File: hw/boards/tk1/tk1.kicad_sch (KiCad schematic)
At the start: 0 parts

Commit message: TK-1 release
* Add dimensions for PCB
* Add layer stackup for PCB
* Change PCB component origin to match expanded board
* Change schematic title to 'TK-1', update release date
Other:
- note added: "Tillitis TK-1"
- note removed: "Tillitis TK1"
- title: TK1 -> TK-1
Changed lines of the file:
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@@
   (paper "A4")
   (title_block
-    (title "TK1")
-    (date "2021-09-29")
+    (title "TK-1")
+    (date "2021-11-14")
     (rev "V1")
     (company "Tillitis AB")
@@
     (effects (font (size 1.27 1.27)) (justify left bottom))
   )
-  (text "Tillitis TK1" (at 106.68 24.13 0)
+  (text "Tillitis TK-1" (at 106.68 24.13 0)
     (effects (font (size 6 6) (thickness 0.254) bold) (justify left bottom))
   )
@@
     )
     (path "/00000000-0000-0000-0000-0000611a4eb9/00000000-0000-0000-0000-000061804e06"
-      (reference "TP1") (unit 1) (value "5V") (footprint "TestPoint:TestPoint_Pad_D1.0mm")
+      (reference "TP1") (unit 1) (value "5V") (footprint "mta1:TestPoint_Pad_D1.0mm")
     )
     (path "/00000000-0000-0000-0000-0000611a4eb9/00000000-0000-0000-0000-000061290a70"
-      (reference "TP2") (unit 1) (value "3V3") (footprint "TestPoint:TestPoint_Pad_D1.0mm")
+      (reference "TP2") (unit 1) (value "3V3") (footprint "mta1:TestPoint_Pad_D1.0mm")
     )
     (path "/00000000-0000-0000-0000-0000611a4eb9/00000000-0000-0000-0000-000061293ed2"
-      (reference "TP3") (unit 1) (value "2V5") (footprint "TestPoint:TestPoint_Pad_D1.0mm")
+      (reference "TP3") (unit 1) (value "2V5") (footprint "mta1:TestPoint_Pad_D1.0mm")
     )
     (path "/00000000-0000-0000-0000-0000611a4eb9/00000000-0000-0000-0000-0000612c6885"
-      (reference "TP4") (unit 1) (value "1V2") (footprint "TestPoint:TestPoint_Pad_D1.0mm")
+      (reference "TP4") (unit 1) (value "1V2") (footprint "mta1:TestPoint_Pad_D1.0mm")
     )
     (path "/00000000-0000-0000-0000-0000611cc101/ab35f289-cbe7-449b-a15d-459a3b4e9240"
-      (reference "TP5") (unit 1) (value "APP_GND") (footprint "TestPoint:TestPoint_Pad_D1.0mm")
+      (reference "TP5") (unit 1) (value "APP_GND") (footprint "mta1:TestPoint_Pad_D1.0mm")
     )
     (path "/00000000-0000-0000-0000-00006161400b/fb64afad-a905-4f4b-98a2-d21a64bd12f3"
-      (reference "TP6") (unit 1) (value "INT_TX") (footprint "TestPoint:TestPoint_Pad_D1.0mm")
+      (reference "TP6") (unit 1) (value "INT_TX") (footprint "mta1:TestPoint_Pad_D1.0mm")
     )
     (path "/00000000-0000-0000-0000-00006161400b/1f54ffea-0a26-464d-98d4-30979db7344f"
-      (reference "TP7") (unit 1) (value "INT_RX") (footprint "TestPoint:TestPoint_Pad_D1.0mm")
+      (reference "TP7") (unit 1) (value "INT_RX") (footprint "mta1:TestPoint_Pad_D1.0mm")
     )
     (path "/00000000-0000-0000-0000-00006161400b/74f30866-0d52-4558-88d9-da85c982a4ac"
-      (reference "TP8") (unit 1) (value "INT_RTS") (footprint "TestPoint:TestPoint_Pad_D1.0mm")
+      (reference "TP8") (unit 1) (value "INT_RTS") (footprint "mta1:TestPoint_Pad_D1.0mm")
     )
     (path "/00000000-0000-0000-0000-00006161400b/d9fa1bba-ba87-4376-952a-41bb8392f957"
-      (reference "TP9") (unit 1) (value "INT_CTS") (footprint "TestPoint:TestPoint_Pad_D1.0mm")
+      (reference "TP9") (unit 1) (value "INT_CTS") (footprint "mta1:TestPoint_Pad_D1.0mm")
     )
     (path "/00000000-0000-0000-0000-0000611cc101/b84f4f68-cc10-43a0-962e-10a1890e7eaf"
-      (reference "TP12") (unit 1) (value "APP_ICE_SCK") (footprint "TestPoint:TestPoint_Pad_D1.0mm")
+      (reference "TP12") (unit 1) (value "APP_ICE_SCK") (footprint "mta1:TestPoint_Pad_D1.0mm")
     )
     (path "/00000000-0000-0000-0000-0000611cc101/f77c0061-34af-41f5-8a00-bb8ae07fe922"
-      (reference "TP13") (unit 1) (value "APP_ICE_SS") (footprint "TestPoint:TestPoint_Pad_D1.0mm")
+      (reference "TP13") (unit 1) (value "APP_ICE_SS") (footprint "mta1:TestPoint_Pad_D1.0mm")
     )
     (path "/00000000-0000-0000-0000-0000611cc101/3c9864fc-0a77-4fe0-8c96-c0260a516ba1"
-      (reference "TP14") (unit 1) (value "APP_ICE_MOSI") (footprint "TestPoint:TestPoint_Pad_D1.0mm")
+      (reference "TP14") (unit 1) (value "APP_ICE_MOSI") (footprint "mta1:TestPoint_Pad_D1.0mm")
     )
     (path "/00000000-0000-0000-0000-0000611cc101/0f9d611d-221f-42fe-a161-07c0ff52c542"
-      (reference "TP15") (unit 1) (value "APP_ICE_MISO") (footprint "TestPoint:TestPoint_Pad_D1.0mm")
+      (reference "TP15") (unit 1) (value "APP_ICE_MISO") (footprint "mta1:TestPoint_Pad_D1.0mm")
     )
     (path "/00000000-0000-0000-0000-0000611cc101/d7bf813c-bb4e-4ed8-b86f-d9ec1d86656d"
-      (reference "TP16") (unit 1) (value "APP_CRESET") (footprint "TestPoint:TestPoint_Pad_D1.0mm")
+      (reference "TP16") (unit 1) (value "APP_CRESET") (footprint "mta1:TestPoint_Pad_D1.0mm")
     )
     (path "/00000000-0000-0000-0000-0000611cc101/32f54cf3-1e0f-4aaa-b508-267b9568217c"
-      (reference "TP17") (unit 1) (value "APP_CDONE") (footprint "TestPoint:TestPoint_Pad_D1.0mm")
+      (reference "TP17") (unit 1) (value "APP_CDONE") (footprint "mta1:TestPoint_Pad_D1.0mm")
     )
     (path "/00000000-0000-0000-0000-0000611cc101/e7d44998-7d27-4371-9f3d-0a968eddee9d"
-      (reference "TP18") (unit 1) (value "APP_GPIO1") (footprint "TestPoint:TestPoint_Pad_D1.0mm")
+      (reference "TP18") (unit 1) (value "APP_GPIO1") (footprint "mta1:TestPoint_Pad_D1.0mm")
     )
     (path "/00000000-0000-0000-0000-0000611cc101/855a271d-d14e-4340-88ef-5eb1d2805d77"
-      (reference "TP19") (unit 1) (value "APP_GPIO2") (footprint "TestPoint:TestPoint_Pad_D1.0mm")
+      (reference "TP19") (unit 1) (value "APP_GPIO2") (footprint "mta1:TestPoint_Pad_D1.0mm")
     )
     (path "/00000000-0000-0000-0000-0000611cc101/8aa5c85f-46b3-4ac4-bd48-3e3352ebb3f6"
-      (reference "TP20") (unit 1) (value "APP_GPIO3") (footprint "TestPoint:TestPoint_Pad_D1.0mm")
+      (reference "TP20") (unit 1) (value "APP_GPIO3") (footprint "mta1:TestPoint_Pad_D1.0mm")
     )
     (path "/00000000-0000-0000-0000-0000611cc101/a6d52094-2dbe-49fa-99c1-8b125d3ae4c6"
-      (reference "TP21") (unit 1) (value "APP_GPIO4") (footprint "TestPoint:TestPoint_Pad_D1.0mm")
+      (reference "TP21") (unit 1) (value "APP_GPIO4") (footprint "mta1:TestPoint_Pad_D1.0mm")
     )
     (path "/00000000-0000-0000-0000-0000611a4eb9/f74c1147-0f6c-4852-95d4-43a254720c79"
-      (reference "TP28") (unit 1) (value "GND") (footprint "TestPoint:TestPoint_Pad_D1.0mm")
+      (reference "TP28") (unit 1) (value "GND") (footprint "mta1:TestPoint_Pad_D1.0mm")
     )
     (path "/00000000-0000-0000-0000-0000611a4eb9/00000000-0000-0000-0000-00006126a5e3"

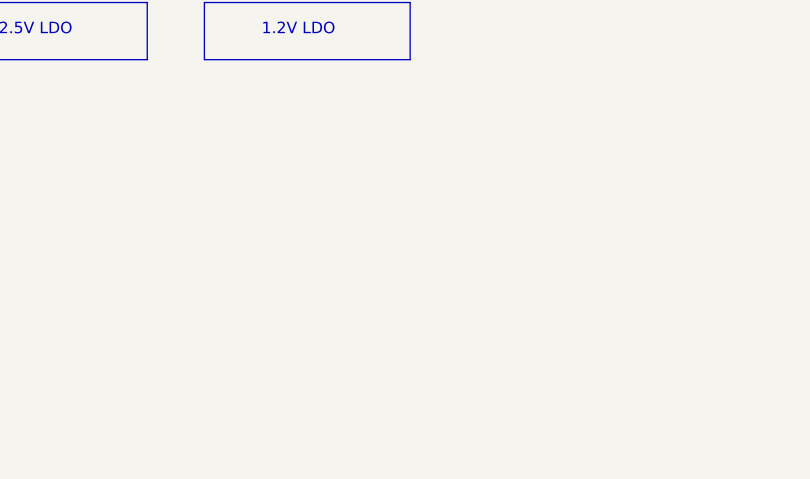
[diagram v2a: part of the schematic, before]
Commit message: TK-1: RevA.1 release
* Add two fiducials to TK-1 board
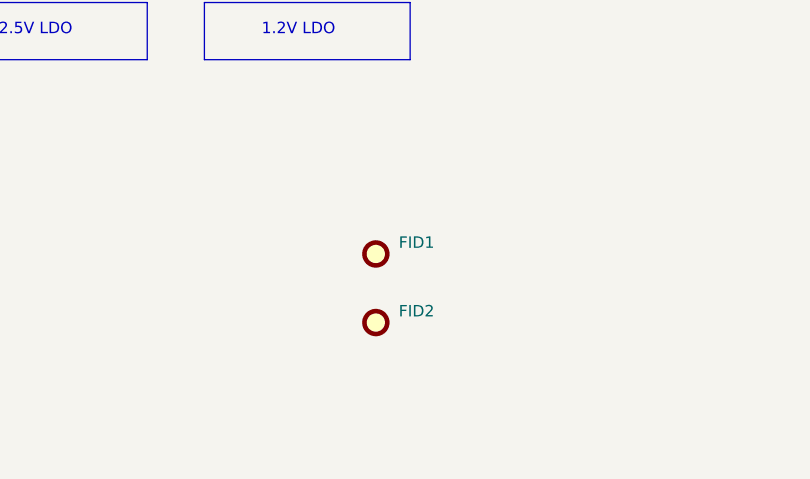
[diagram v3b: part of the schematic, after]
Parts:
- added FID1, FID2: (no value), symbol Mechanical:Fiducial
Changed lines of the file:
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@@
     (effects (font (size 1.27 1.27)) (justify left bottom))
+  )
+  (symbol (lib_id "Mechanical:Fiducial") (at 124.46 163.83 90) (unit 1)
+    (in_bom no) (on_board yes) (fields_autoplaced)
+    (property "Reference" "FID1" (id 0) (at 127 162.5599 90)
+      (effects (font (size 1.27 1.27)) (justify right))
+    )
+    (property "Value" "" (id 1) (at 127 165.0999 90)
+      (effects (font (size 1.27 1.27)) (justify right))
+    )
+    (property "Footprint" "" (id 2) (at 124.46 163.83 0)
+      (effects (font (size 1.27 1.27)) hide)
+    )
+    (property "Datasheet" "~" (id 3) (at 124.46 163.83 0)
+      (effects (font (size 1.27 1.27)) hide)
+    )
+  )
+  (symbol (lib_id "Mechanical:Fiducial") (at 124.46 171.45 90) (unit 1)
+    (in_bom no) (on_board yes) (fields_autoplaced)
+    (property "Reference" "FID2" (id 0) (at 127 170.1799 90)
+      (effects (font (size 1.27 1.27)) (justify right))
+    )
+    (property "Value" "" (id 1) (at 127 172.7199 90)
+      (effects (font (size 1.27 1.27)) (justify right))
+    )
+    (property "Footprint" "" (id 2) (at 124.46 171.45 0)
+      (effects (font (size 1.27 1.27)) hide)
+    )
+    (property "Datasheet" "~" (id 3) (at 124.46 171.45 0)
+      (effects (font (size 1.27 1.27)) hide)
+    )
   )
   (sheet (at 43.18 180.34) (size 12.7 3.81) (fields_autoplaced)
@@
       (reference "FB3") (unit 1) (value "BLM18KG300TN1D") (footprint "mta1:Ferritbead_0603_1608Metric")
     )
+    (path "/59501395-780b-47e4-8967-9f965674a799"
+      (reference "FID1") (unit 1) (value "Fiducial") (footprint "Fiducial:Fiducial_0.75mm_Mask1.5mm")
+    )
+    (path "/bf741fd1-5855-4a31-8c21-db9bc5f783af"
+      (reference "FID2") (unit 1) (value "Fiducial") (footprint "Fiducial:Fiducial_0.75mm_Mask1.5mm")
+    )
     (path "/00000000-0000-0000-0000-00006161400b/7b422c5e-fd7b-4ac9-8400-966a18c34fdc"
